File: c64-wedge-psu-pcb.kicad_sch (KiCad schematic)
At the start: 22 parts, among them U1 LM2576T-ADJ

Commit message: updates
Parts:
- C1: footprint Capacitor_THT:CP_Radial_D16.0mm_P7.50mm -> Capacitor_THT:CP_Radial_D18.0mm_P7.50mm
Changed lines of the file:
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@@
 			)
 		)
-		(property "Footprint" "Capacitor_THT:CP_Radial_D16.0mm_P7.50mm"
+		(property "Footprint" "Capacitor_THT:CP_Radial_D18.0mm_P7.50mm"
 			(at 93.6752 104.14 0)
 			(effects
@@
 			)
 		)
-		(property "Description" "UHE1E472MHD"
+		(property "Description" "UHW1E472MHD"
 			(at 92.71 100.33 0)
 			(effects

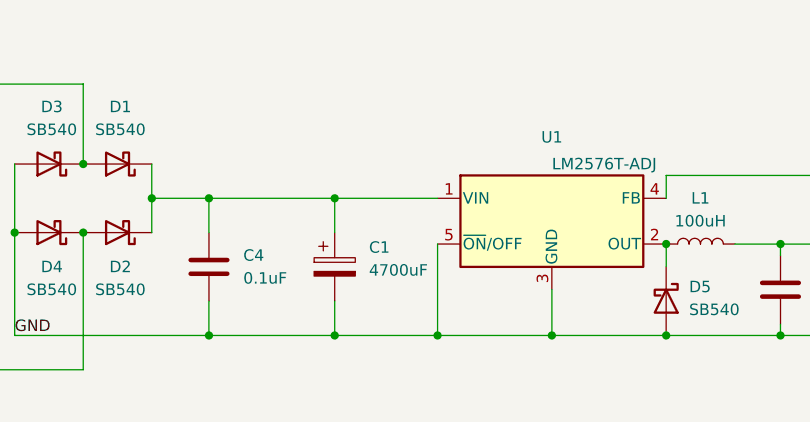
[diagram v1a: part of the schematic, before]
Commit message: Upgrade C1 to 5600uF and C2 to a better part, add some notes
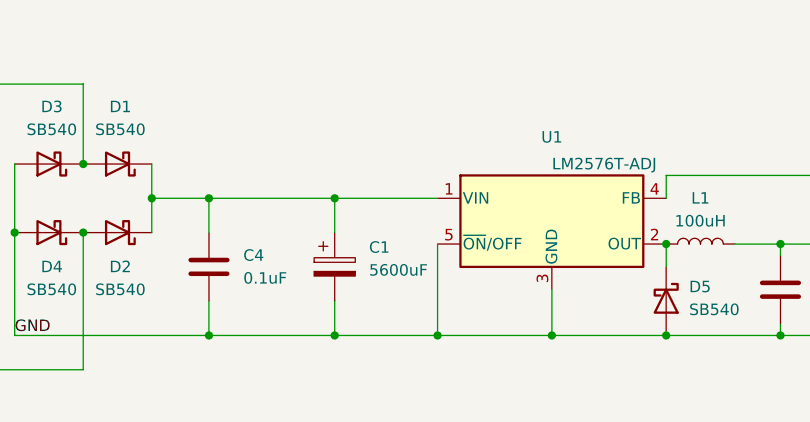
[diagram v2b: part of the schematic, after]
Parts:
- C1: value 4700uF -> 5600uF; Note (none) -> Footprint has 18mm diameter, even though the part is 16mm (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
- R1, R2, R3: Note (none) -> 1% Metal Film (1/4 W)
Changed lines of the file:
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@@
 			)
 		)
-		(property "Description" "UPW1E222MHD"
+		(property "Description" "UHW1E222MHD6"
 			(at 153.67 102.87 0)
 			(effects
@@
 			)
 		)
+		(property "Note" "1% Metal Film (1/4 W)"
+			(at 231.14 101.6 90)
+			(effects
+				(font
+					(size 1.27 1.27)
+				)
+				(hide yes)
+			)
+		)
 		(pin "1"
 		)
@@
 			)
 		)
+		(property "Note" "1% Metal Film (1/4 W)"
+			(at 148.59 93.98 0)
+			(effects
+				(font
+					(size 1.27 1.27)
+				)
+				(hide yes)
+			)
+		)
 		(pin "1"
 		)
@@
 			)
 		)
-		(property "Value" "4700uF"
+		(property "Value" "5600uF"
 			(at 96.52 100.7109 0)
 			(effects
@@
 			)
 		)
-		(property "Description" "UHW1E472MHD"
+		(property "Description" "UHW1E562MHD"
+			(at 92.71 100.33 0)
+			(effects
+				(font
+					(size 1.27 1.27)
+				)
+				(hide yes)
+			)
+		)
+		(property "Note" "Footprint has 18mm diameter, even though the part is 16mm (to allow replacement for a bigger part)"
 			(at 92.71 100.33 0)
 			(effects
@@
 			(effects
 				(font
+					(size 1.27 1.27)
+				)
+				(hide yes)
+			)
+		)
+		(property "Note" "1% Metal Film (1/4 W)"
+			(at 152.4 90.17 90)
+			(effects
+				(font

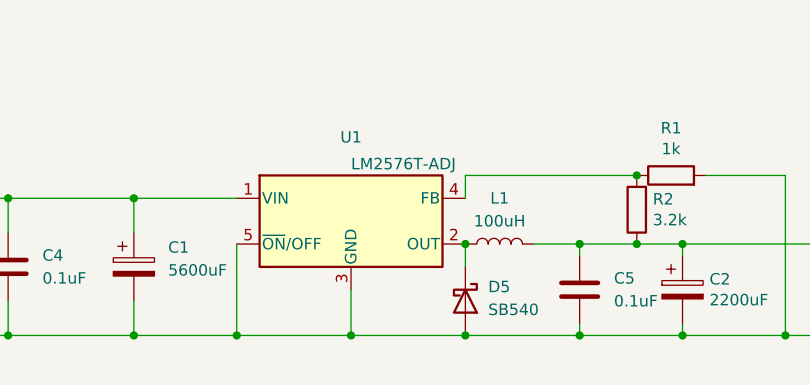
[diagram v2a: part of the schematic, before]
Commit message: Add heatsink
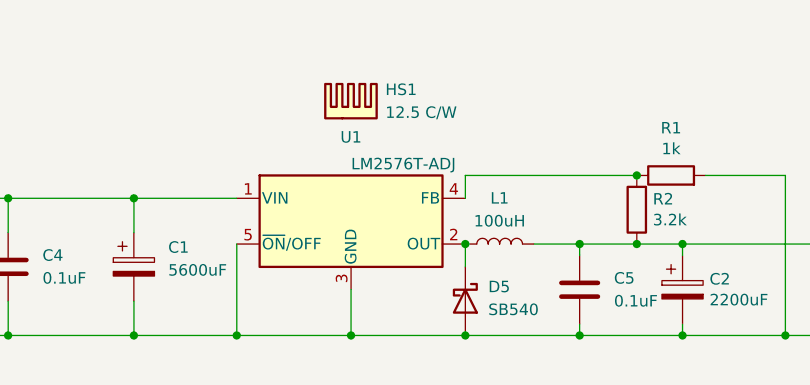
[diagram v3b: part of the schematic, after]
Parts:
- added HS1: 12.5 C/W, symbol Mechanical:Heatsink
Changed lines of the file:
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@@
+		)
+	)
+	(symbol
+		(lib_id "Mechanical:Heatsink")
+		(at 116.84 83.82 0)
+		(unit 1)
+		(exclude_from_sim yes)
+		(in_bom yes)
+		(on_board no)
+		(dnp no)
+		(fields_autoplaced yes)
+		(property "Reference" "HS1"
+			(at 120.65 80.6449 0)
+			(effects
+				(font
+					(size 1.27 1.27)
+				)
+				(justify left)
+			)
+		)
+		(property "Value" "12.5 C/W"
+			(at 120.65 83.1849 0)
+			(effects
+				(font
+					(size 1.27 1.27)
+				)
+				(justify left)
+			)
+		)
+		(property "Footprint" ""
+			(at 117.1448 83.82 0)
+			(effects
+				(font
+					(size 1.27 1.27)
+				)
+				(hide yes)
+			)
+		)
+		(property "Datasheet" "~"
+			(at 117.1448 83.82 0)
+			(effects
+				(font
+					(size 1.27 1.27)
+				)
+				(hide yes)
+			)
+		)
+		(property "Description" "Heatsink ATS-PCB1035 (TO-220)"
+			(at 116.84 83.82 0)
+			(effects
+				(font
+					(size 1.27 1.27)
+				)
+				(hide yes)
+			)
+		)
+		(property "Note" "Screw it on the LM2576, use thermal paste (for example Noctua NT-H1)"
+			(at 116.84 83.82 0)
+			(effects
+				(font
+					(size 1.27 1.27)
+				)
+				(hide yes)
+			)
+		)
+		(instances
+			(project ""
+				(path "/25ef7e59-af8f-4cb3-8d4a-791b61806d46"
+					(reference "HS1")
+					(unit 1)
+				)
+			)
 		)
 	)
